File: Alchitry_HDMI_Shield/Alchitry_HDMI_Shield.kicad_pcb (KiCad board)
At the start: 2 copper layers, 65 x 45 mm, 26 parts, among them J1 HDMI_A_1.4, U1 boardmezzanine_new, U3 TFP410

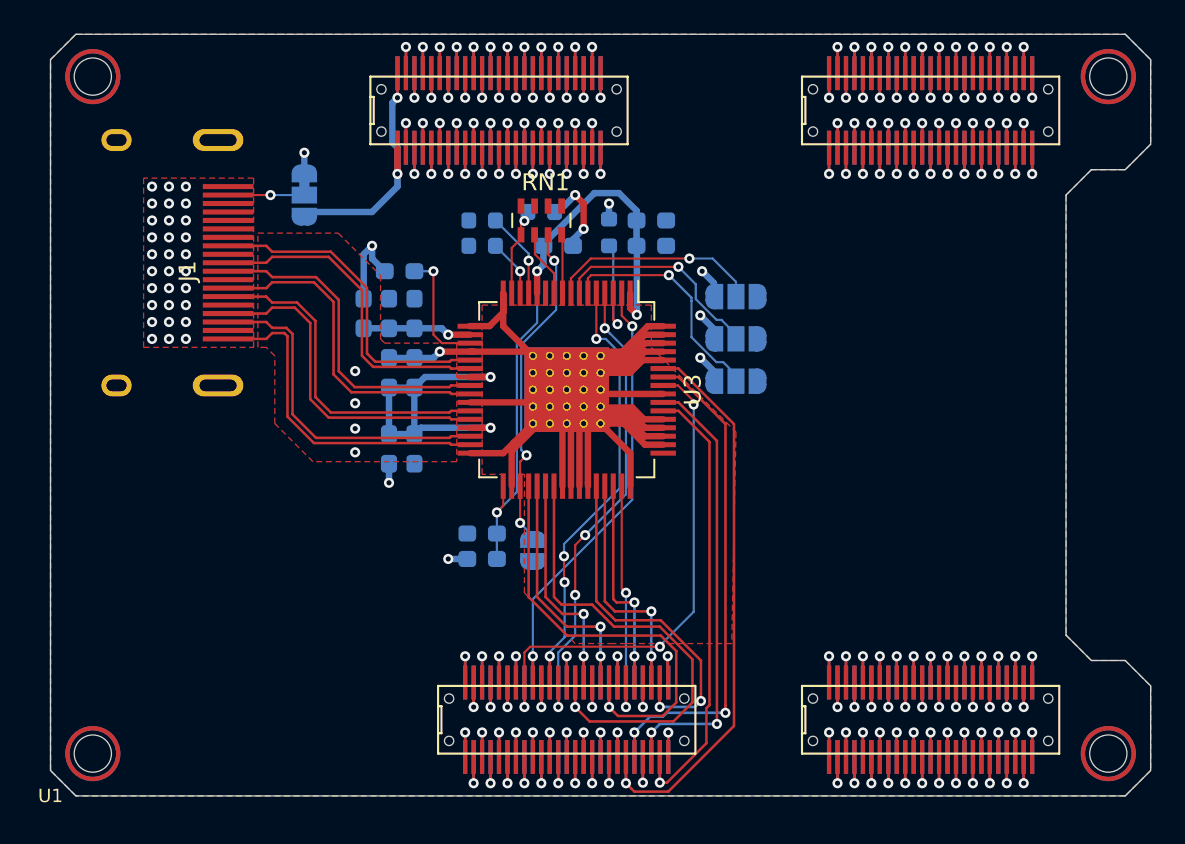
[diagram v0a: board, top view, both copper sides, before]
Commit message: updated shield v4 schematic
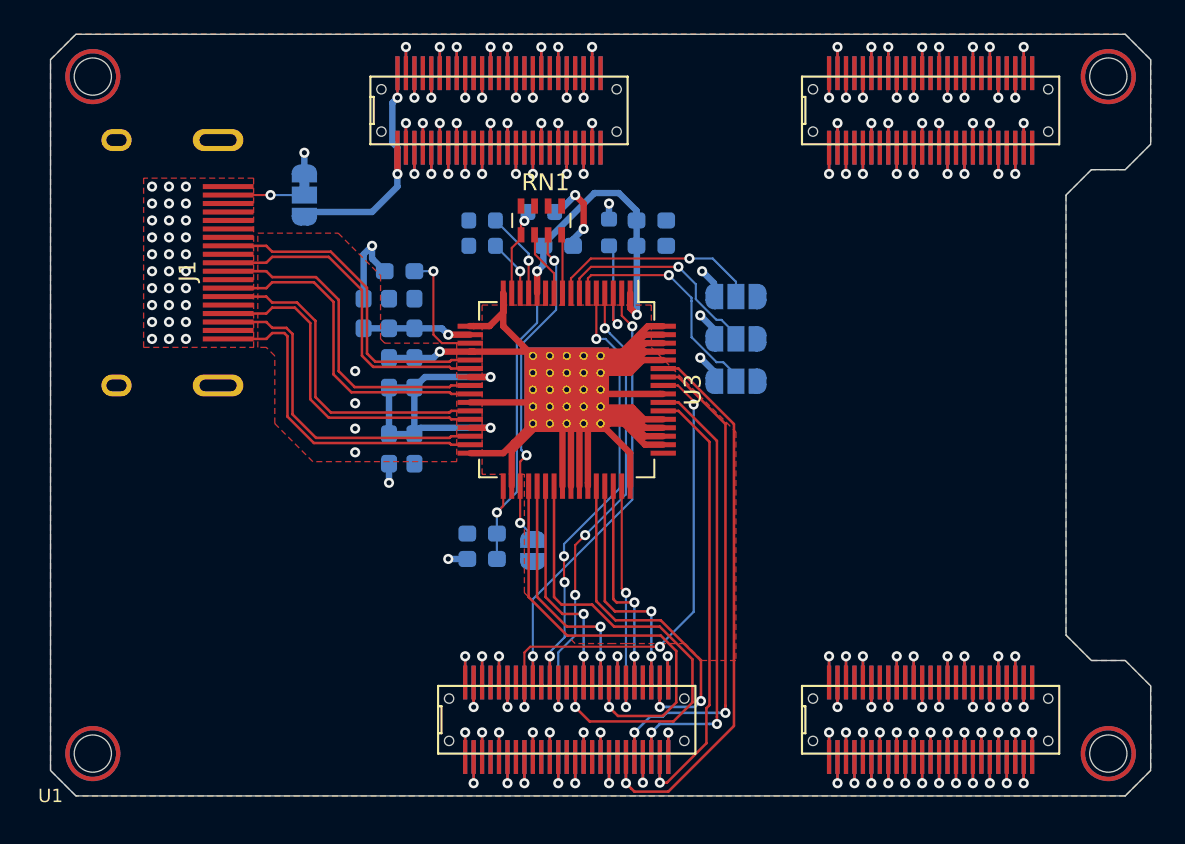
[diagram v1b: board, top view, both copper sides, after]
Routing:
- net GNDREF: track 193.6 -> 119.8 mm, vias 69 -> 44
- net +3V3: track 100.3 -> 29.5 mm, vias 37 -> 13
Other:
- net class Default removed
- net class pwr removed
